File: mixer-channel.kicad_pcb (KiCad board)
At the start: 2 copper layers, 30 x 128 mm, 107 parts, among them J101 Conn_02x08_Odd_Even, J102 Conn_02x04_Counter_Clockwise, SW101 SW_4PDT_x4, U101 TL074, U102 TL074, U103 TL074, U301 TL074, U302 TL074, U401 TL074, U402 LM3916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

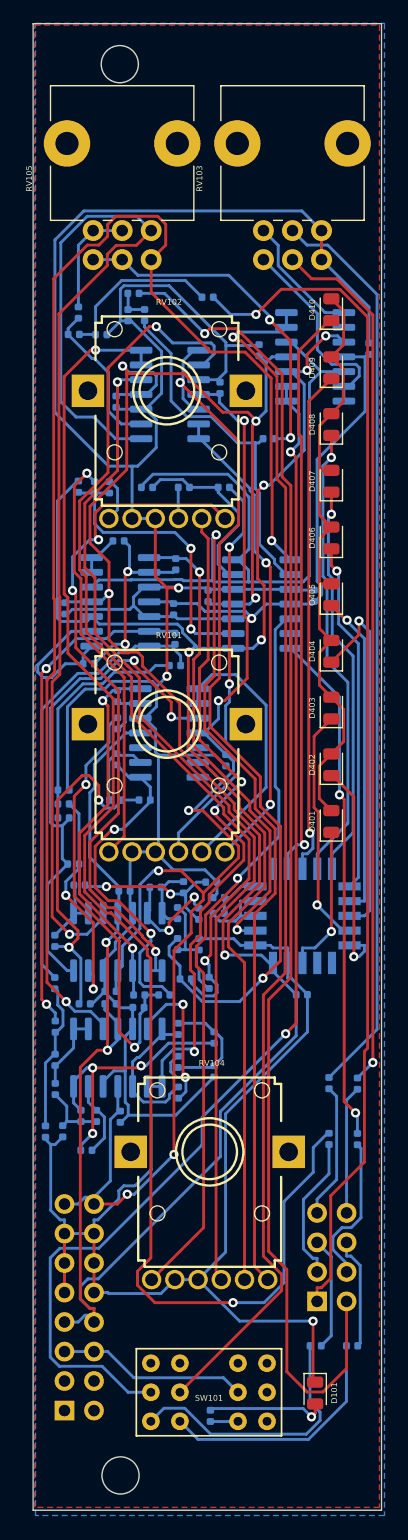
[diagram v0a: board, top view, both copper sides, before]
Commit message: Stop cue button from shorting against mounting rails
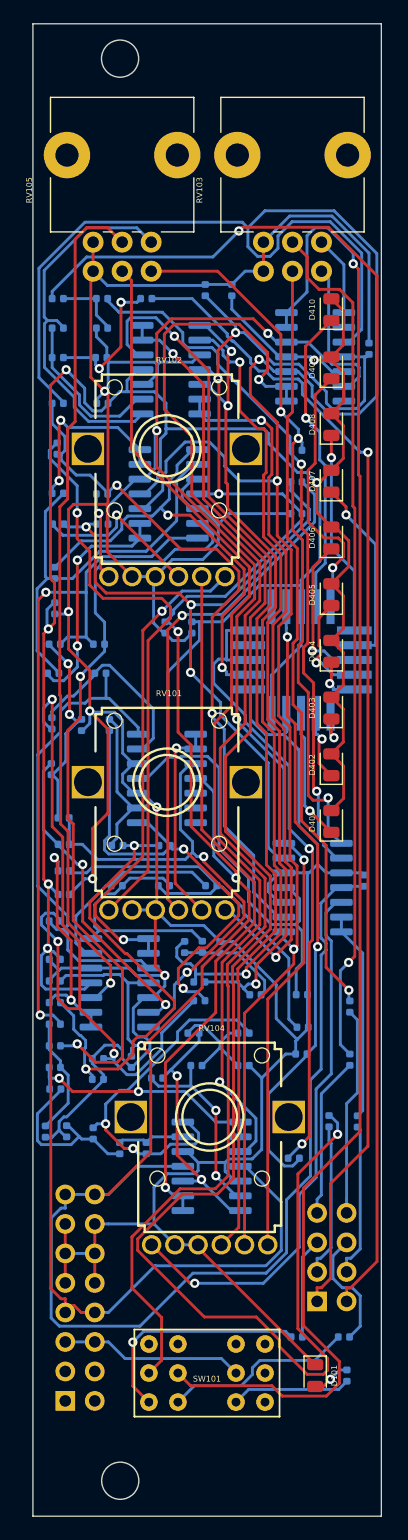
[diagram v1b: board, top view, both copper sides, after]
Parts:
- R110, R111: value 10k -> 50k
- R405: value 7.5k -> 3.8k
- U402: footprint Package_LCC:PLCC-20 -> Package_LCC:PLCC-20-LongPads
- moved U102 24.8 mm to (60.3, 113.2)
- moved R404 22.1 mm to (58.7, 136.5)
- moved U402 22.0 mm to (59.3, 93.6)
- moved C302 15.8 mm to (64.7, 112.6), turned to 90 degrees
- moved R405 15.2 mm to (59.3, 127.5)
- moved C306 14.8 mm to (59.4, 125.2)
- moved U403 12.4 mm to (51.6, 137.2), turned to 180 degrees
- moved R104 12.2 mm to (63.2, 155.2)
- moved R113 11.3 mm to (38.4, 81.9)
- moved R411 10.5 mm to (38.1, 92.2)
- moved R403 10.4 mm to (38.1, 86.1)
- moved U401 10.2 mm to (47.9, 79.3)
- moved C311 9.66 mm to (38.1, 116.1)
- moved C106 8.51 mm to (51.1, 61.8)
- moved R103 7.39 mm to (38.4, 71.5), turned to 180 degrees
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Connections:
- D401 pad 2: Net-(D401-Pad2) -> VDD
- D402 pad 2: Net-(D401-Pad2) -> VDD
- D403 pad 2: Net-(D401-Pad2) -> VDD
- D404 pad 2: Net-(D401-Pad2) -> VDD
- D405 pad 2: Net-(D401-Pad2) -> VDD
- D406 pad 2: Net-(D401-Pad2) -> VDD
- D407 pad 2: Net-(D401-Pad2) -> VDD
- D408 pad 2: Net-(D401-Pad2) -> VDD
- D409 pad 2: Net-(D401-Pad2) -> VDD
- D410 pad 2: Net-(D401-Pad2) -> VDD
- RV105 pad 1: /L -> GND
- RV105 pad 2: Net-(R110-Pad1) -> /L
- RV105 pad 4: /R -> GND
- RV105 pad 5: Net-(R111-Pad1) -> /R
- U102 pad 8: /R -> Net-(R111-Pad1)
- U103 pad 1: /L -> Net-(R110-Pad1)
- U402 pad 10: Net-(D410-Pad1) -> Net-(R404-Pad2)
- U402 pad 11: Net-(D409-Pad1) -> VDD
- U402 pad 12: Net-(D408-Pad1) -> Net-(D410-Pad1)
- U402 pad 13: Net-(D407-Pad1) -> Net-(D409-Pad1)
- U402 pad 14: Net-(D406-Pad1) -> Net-(D408-Pad1)
- U402 pad 15: Net-(D405-Pad1) -> Net-(D407-Pad1)
- U402 pad 16: Net-(D404-Pad1) -> Net-(D406-Pad1)
- U402 pad 17: Net-(D403-Pad1) -> Net-(D405-Pad1)
- U402 pad 18: Net-(D402-Pad1) -> Net-(D404-Pad1)
- U402 pad 19: (no net) -> Net-(D403-Pad1)
- U402 pad 20: (no net) -> Net-(D402-Pad1)
- U402 pad 7: Net-(R404-Pad1) -> (no net)
- U402 pad 8: Net-(R404-Pad2) -> Net-(R404-Pad1)
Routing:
- net VDD: track 223.2 -> 311.3 mm, vias 7 -> 6
- net VSS: track 159.9 -> 234.0 mm, vias 7 -> 6
- net /VU_L: track 124.8 -> 194.6 mm, vias 5 -> 3
- net Net-(D401-Pad2): track 52.1 -> 0.00 mm
- net Net-(R404-Pad2): track 4.42 -> 53.2 mm, vias 0 -> 2
- net Net-(R404-Pad1): track 6.72 -> 54.4 mm, vias 0 -> 2
- net Net-(R107-Pad1): track 16.0 -> 59.7 mm, vias 0 -> 3
- net Net-(R101-Pad1): track 25.3 -> 59.3 mm
- net Net-(R111-Pad1): track 29.9 -> 62.3 mm, vias 2 -> 3
- net Net-(R109-Pad1): track 30.3 -> 60.5 mm, vias 0 -> 2
- net /R: track 116.6 -> 86.7 mm, vias 2 -> 1
- net Net-(D404-Pad1): track 31.8 -> 4.35 mm
- net Net-(R119-Pad2): track 45.4 -> 18.1 mm, vias 2 -> 0
- net /L: track 100.9 -> 73.6 mm
- net Net-(SW101-Pad5): track 104.3 -> 129.8 mm
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- removed copper zone on B.Cu, net GND
- removed copper zone on F.Cu, net GND
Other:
- board size 30 x 128 mm -> 30 x 128.5 mm
- board text added: "SEND HP OUT IN"
- board text added: "VSS GND GND GND VDD 5V NC NC"
